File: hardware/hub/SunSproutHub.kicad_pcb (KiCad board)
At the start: 6 copper layers, 56 x 85 mm, 142 parts, among them CN5 1755736, J2 Conn_01x02, J201 RJHSE5380, J202 RJHSE5380, J203 Qwiic, J302 JST_PA_S02B-PASK-2, J4 BATTERY, J401 JST_PA_S02B-PASK-2, J6 Qwiic, J7 GPIO_HEADER_L, J8 GPIO_HEADER_R, Q1 MDD3415, Q2 DMP3098L-7, Q3 AO3400A, Q301 AO3400A, Q302 AO3400A, Q303 AO3400A, Q304 AO3400A, SW1 SW_Push, SW2 SW_Push, SW3 SW_Push, U1 ESP32-C5-WROOM-1U, U201 PCA9615, U3 BQ34Z100PWR-G1, U4 TPS631000, U5 TPS22918DBVR, U8 BQ25798RQMR

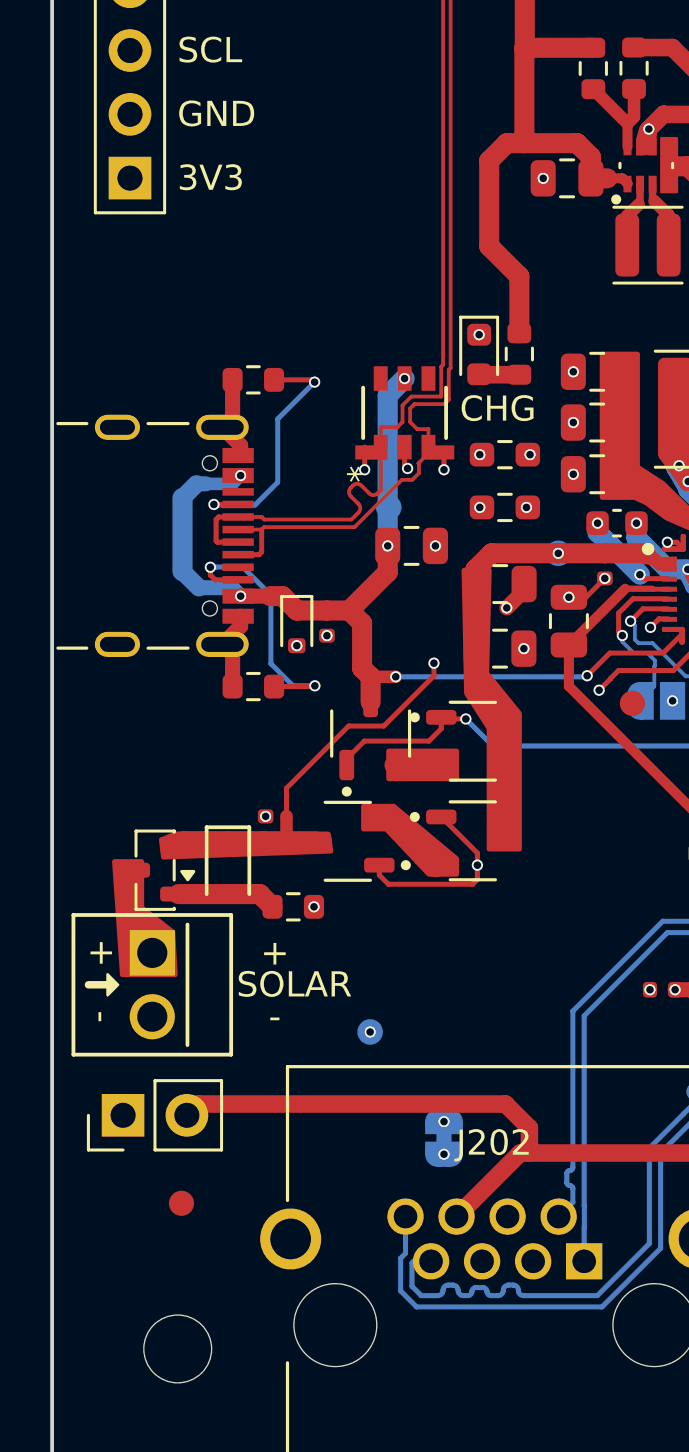
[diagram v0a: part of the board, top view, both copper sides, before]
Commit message: hardware(hub): J2 gets a 3V3_SYS pin next to VCC_2, docs explain why
J2 (VCC_2 INJ) grows from two pins to three: GRN_N, VCC_2 and the always-on
3V3_SYS rail. A jumper from 3V3_SYS to VCC_2 feeds a second satellite from the
hub, and the pin lets test clips power the board at 3.3 V instead of USB.

The header moves and is rotated, with its routing and zones updated.
The buffer module doc describes the pinout and both uses, and warns to cut
JP2 first. Neither use is tested yet.
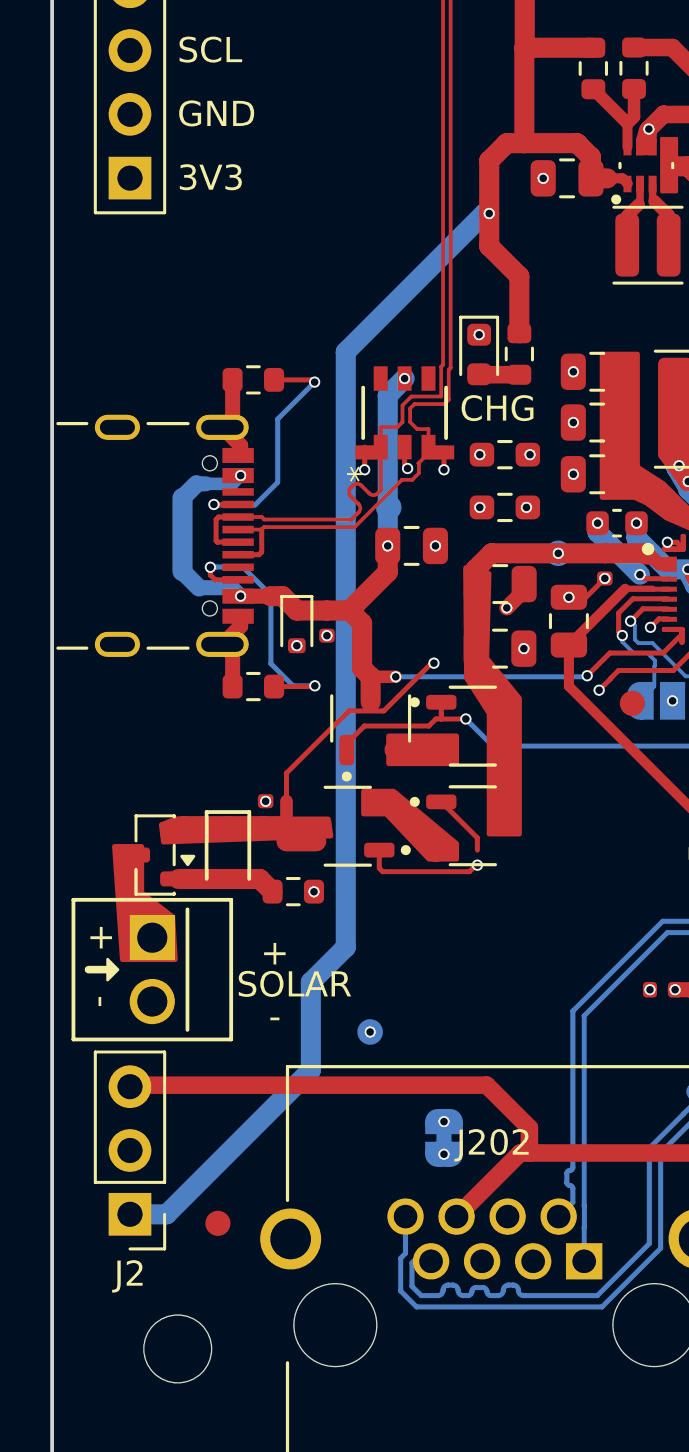
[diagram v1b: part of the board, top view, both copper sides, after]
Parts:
- J2: value Conn_01x02 -> Conn_01x03; footprint Connector_PinHeader_2.54mm:PinHeader_1x02_P2.54mm_Vertical -> Connector_PinHeader_2.54mm:PinHeader_1x03_P2.54mm_Vertical
- moved J2 3.95 mm to (28.1, 99.6), turned to 180 degrees
- moved Fid8 1.66 mm to (31.6, 100.0)
- moved C28 0.60 mm to (33.5, 83.7)
- moved D2 0.60 mm to (32.0, 85.2)
- moved R19 0.60 mm to (34.6, 86.8)
- moved CN5 0.60 mm to (29.0, 89.9)
- moved Q2 0.60 mm to (29.1, 85.3)
- moved NT3 0.60 mm to (34.3, 83.7)
- moved Q302 0.60 mm to (41.7, 80.2)
- moved Q303 0.60 mm to (36.8, 84.2)
- moved Q304 0.60 mm to (41.7, 84.2)
- moved Q301 0.60 mm to (37.7, 79.9)
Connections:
- J2 pad 1: GRN_P -> 3V3_SYS
- J2 pad 2: GRN_N -> GRN_P
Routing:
- net 3V3_SYS: track 131.9 -> 178.6 mm, vias 4 -> 5
- net GRN_N: track 38.1 -> 39.8 mm
- net GRN_P: track 58.9 -> 58.0 mm
- net /BQ25798 Charger/VAC2_DET: track 19.5 -> 19.0 mm
